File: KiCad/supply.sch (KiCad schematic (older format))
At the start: 75 parts, among them IC10 AP62301Z6-7, IC12 74HC00PW, IC13 SN74LVC1G126DCKR, IC3 TPS54561, IC4 TPS7A0518PDBVT, IC8 LM3671MF-3.3, IC9 LM3671MF-3.3, T3 BSS138APW

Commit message: Replace 5V0 and 3V3 DCDC
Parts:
- removed C16, C17, C18: C_47u_0805, jetson-nano-baseboard-footprints:0805-cap, symbol jetson-nano-baseboard:C_47u_0805
- removed C19: C_100n_0402, jetson-nano-baseboard-footprints:0402-cap, symbol jetson-nano-baseboard:C_100n_0402
- removed C20, C59, C61: C_22u_0603, antmicro-footprints:0603-cap, symbol antmicroCapacitors0603:C_22u_0603
- removed C21, C22, C23: C_2u2_1206, jetson-nano-baseboard-footprints:1206-cap, symbol jetson-nano-baseboard:C_2u2_1206
- removed C24: C_10n_0402, jetson-nano-baseboard-footprints:0402-cap, symbol jetson-nano-baseboard:C_10n_0402
- removed C25: C_4n7_0402, jetson-nano-baseboard-footprints:0402-cap, symbol jetson-nano-baseboard:C_4n7_0402
- removed C28: C_100n_0402, antmicro-footprints:0402-cap, symbol antmicroCapacitors0402:C_100n_0402
- removed C55, C57: C_2u2_0402, jetson-nano-baseboard-footprints:0402-cap, symbol jetson-nano-baseboard:C_2u2_0402
- removed C56, C58: C_10u_0603, jetson-nano-baseboard-footprints:0603-cap, symbol jetson-nano-baseboard:C_10u_0603
- removed C64: C_47p_0402, jetson-nano-baseboard-footprints:0402-cap, symbol jetson-nano-baseboard:C_47p_0402
- removed D1: PDS760-13, jetson-nano-baseboard-footprints:PowerDI, symbol jetson-nano-baseboard:Diode_Schottky
- removed FB1: 742792022, antmicro-footprints:0805-cap, symbol Device:Ferrite_Bead_Small
- removed IC10: AP62301Z6-7, antmicro-footprints:SOT-563, symbol antmicroDCDCConverters:AP62301Z6-7
- removed IC3: TPS54561, jetson-nano-baseboard-footprints:WSON-10_4x4, symbol jetson-nano-baseboard:TPS54561
- removed IC8, IC9: LM3671MF-3.3, jetson-nano-baseboard-footprints:SOT23-5N, symbol jetson-nano-baseboard:LM3671
- removed L1: WE_7447798720, jetson-nano-baseboard-footprints:WE_7447798720, symbol jetson-nano-baseboard:WE_7447798720
- removed L4, L6: LQH32PN2R2NN0L, jetson-nano-baseboard-footprints:LQH32PN2R2NN0L, symbol jetson-nano-baseboard:LQH32PN2R2NN0L
- removed L5: XEL4030-332MEC, antmicro-footprints:Coilcraft-XEL4030, symbol antmicroFixedInductors:XEL4030-332MEC
- removed R134: R_33k2_0402, antmicro-footprints:0402-res, symbol antmicroResistors0402:R_33k2_0402
- removed R44: R_243k_0402, jetson-nano-baseboard-footprints:0402-res, symbol jetson-nano-baseboard:R_243k_0402
- removed R45: R_49R9_0402, jetson-nano-baseboard-footprints:0402-res, symbol jetson-nano-baseboard:R_49R9_0402
- removed R46: R_53k6_0402, jetson-nano-baseboard-footprints:0402-res, symbol jetson-nano-baseboard:R_53k6_0402
- removed R48: R_16k9_0402, jetson-nano-baseboard-footprints:0402-res, symbol jetson-nano-baseboard:R_16k9_0402
- removed R52: R_10k2_0402, jetson-nano-baseboard-footprints:0402-res, symbol jetson-nano-baseboard:R_10k2_0402
- removed R74: R_0R_0402, antmicro-footprints:0402-res, symbol antmicroResistors0402:R_0R_0402
- removed R75, R76: R_10k_0402, antmicro-footprints:0402-res, symbol antmicroResistors0402:R_10k_0402
- removed R77: R_100k_0402, jetson-nano-baseboard-footprints:0402-res, symbol jetson-nano-baseboard:R_100k_0402
- removed R89, R91: R_0R_0402, jetson-nano-baseboard-footprints:0402-res, symbol jetson-nano-baseboard:R_0R_0402
- removed R90, R93: R_10k_0402, jetson-nano-baseboard-footprints:0402-res, symbol jetson-nano-baseboard:R_10k_0402
- removed TP41, TP43, TP45, TP5: ~, jetson-nano-baseboard-footprints:TP-R-1.5, symbol jetson-nano-baseboard:Testpad
- added C81, C82: C_4u7_0603, antmicro-footprints:0603-cap, symbol antmicroCapacitors0603:C_4u7_0603
- added C83, C84, C85, C86: C_220n_0603_25V, antmicro-footprints:0603-cap, symbol antmicroCapacitors0603:C_220n_0603_25V
- added C87, C88: C_1u_0402, antmicro-footprints:0402-cap, symbol antmicroCapacitors0402:C_1u_0402
- added C89, C90: C_100n_0402, antmicro-footprints:0402-cap, symbol antmicroCapacitors0402:C_100n_0402
- added C91, C94, C95, C96, C97, C98: C_47u_0603, antmicro-footprints:0603-cap, symbol antmicroCapacitors0603:C_47u_0603
- added C92, C93: C_15p_0402, antmicro-footprints:0402-cap, symbol antmicroCapacitors0402:C_15p_0402
- added FB3, FB4: 742792022, antmicro-footprints:0805-cap, symbol Device:Ferrite_Bead_Small
- added L11: 7447709150, antmicro-footprints:WE_7447709150, symbol antmicroFixedInductors:7447709150
- added L12: 7443251000, antmicro-footprints:WE_7443251000, symbol antmicroFixedInductors:7443251000
- added R117, R94: R_100k_0402, antmicro-footprints:0402-res, symbol antmicroResistors0402:R_100k_0402
- added R118, R120: R_100k_1%_0402, antmicro-footprints:0402, symbol antmicroResistors0402:R_100k_1%_0402
- added R119: R_44k2_0402, antmicro-footprints:0402-res, symbol antmicroResistors0402:R_44k2_0402
- added R121: R_24k9_0.1%_0402, antmicro-footprints:0402-res, symbol antmicroResistors0402:R_24k9_0.1%_0402
- added R?: R_10k_0402, jetson-nano-baseboard-footprints:0402-res, symbol jetson-nano-baseboard:R_10k_0402
- added R?: R_0R_0402, jetson-nano-baseboard-footprints:0402-res, symbol jetson-nano-baseboard:R_0R_0402
- added U1, U2: LM60440AQRPKRQ1, LM60440AQRPKRQ1, symbol antmicroDCDCConverters:LM60440AQRPKRQ1
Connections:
- wire segments 229 -> 192
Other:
- note added: "3V3 DC/DC"
- note added: "3V3/4A"
- note added: "5V DC/DC"
- note added: "5V/4A"
- note removed: "5V/5A"
- note removed: "Bulk load"
- note removed: "Camera #1 3V3"
- note removed: "Camera #2 3V3"
- note removed: "Main DC/DC"
- note removed: "System 3V3"
- moved on the sheet: C60, C65, IC4, R92, TP40, TP47

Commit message: Fix symbols, change DCDCC output capacitors to 0805
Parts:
- removed C91, C94, C95, C96, C97, C98: C_47u_0603, antmicro-footprints:0603-cap, symbol antmicroCapacitors0603:C_47u_0603
- added C? (x6): C_47u_0805, antmicro-footprints:0805-cap, symbol antmicroCapacitorsmisc:C_47u_0805
- gave numbers to parts that had none: 2
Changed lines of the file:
@@
 Wire Wire Line
 	4050 3150 5025 3150
-$Comp
-L antmicroCapacitors0603:C_47u_0603 C94
-U 1 1 619E2469
-P 5150 2025
-F 0 "C94" H 5265 2070 60  0000 L CNN
-F 1 "C_47u_0603" H 5150 1875 60  0001 C CNN
-F 2 "antmicro-footprints:0603-cap" H 5350 2225 60  0001 L CNN
-F 3 "" H 5150 2025 50  0001 C CNN
-F 4 "MURATA" H 5350 2425 60  0001 L CNN "Manufacturer"
-F 5 "GRM188R60J476ME15D" H 5350 2325 60  0001 L CNN "MPN"
-F 6 "47u" H 5265 1972 50  0000 L CNN "Val"
-	1    5150 2025
-	1    0    0    -1
-$EndComp
 Text GLabel 5575 2500 2    50   Input ~ 0
 5V0_SYS
@@
 Text GLabel 5125 1875 0    50   Input ~ 0
 5V0_SYS
-Wire Wire Line
-	5125 1875 5150 1875
-Connection ~ 5150 1875
 $Comp
 L Device:Ferrite_Bead_Small FB4
@@
 	4000 5800 4975 5800
 $Comp
-L antmicroCapacitors0603:C_47u_0603 C91
-U 1 1 61E2F969
-P 4900 4650
-F 0 "C91" H 5015 4695 60  0000 L CNN
-F 1 "C_47u_0603" H 4900 4500 60  0001 C CNN
-F 2 "antmicro-footprints:0603-cap" H 5100 4850 60  0001 L CNN
-F 3 "" H 4900 4650 50  0001 C CNN
-F 4 "MURATA" H 5100 5050 60  0001 L CNN "Manufacturer"
-F 5 "GRM188R60J476ME15D" H 5100 4950 60  0001 L CNN "MPN"
-F 6 "47u" H 5015 4597 50  0000 L CNN "Val"
-	1    4900 4650
-	1    0    0    -1
-$EndComp
-$Comp
 L jetson-nano-baseboard:GND #GND_0163
 U 1 1 61E2F985
@@
 	1975 4850 1550 4850
 Connection ~ 5325 5150
-Wire Wire Line
-	4875 4500 4900 4500
-Connection ~ 4900 4500
 $Comp
 L Device:Ferrite_Bead_Small FB3
@@
 #RESET
 $Comp
-L jetson-nano-baseboard:R_10k_0402 R?
+L jetson-nano-baseboard:R_10k_0402 R44
 U 1 1 620FA0ED
 P 2200 5550
-F 0 "R?" H 2200 5450 60  0000 C CNN
+F 0 "R44" H 2200 5450 60  0000 C CNN
 F 1 "R_10k_0402" H 2200 5400 60  0001 C CNN
 F 2 "jetson-nano-baseboard-footprints:0402-res" H 2400 5750 60  0001 L CNN
@@
 	2350 5550 2675 5550
 $Comp
-L jetson-nano-baseboard:R_0R_0402 R?
+L jetson-nano-baseboard:R_0R_0402 R45
 U 1 1 6216200E
 P 2675 5250
-F 0 "R?" V 2766 5320 60  0000 L CNN
+F 0 "R45" V 2766 5320 60  0000 L CNN
 F 1 "R_0R_0402" H 2675 5100 60  0001 C CNN
 F 2 "jetson-nano-baseboard-footprints:0402-res" H 2875 5450 60  0001 L CNN
@@
 $EndComp
 $Comp
-L antmicroCapacitors0603:C_47u_0603 C96
-U 1 1 61A02D24
-P 5600 2025
-F 0 "C96" H 5715 2070 60  0000 L CNN
-F 1 "C_47u_0603" H 5600 1875 60  0001 C CNN
-F 2 "antmicro-footprints:0603-cap" H 5800 2225 60  0001 L CNN
-F 3 "" H 5600 2025 50  0001 C CNN
-F 4 "MURATA" H 5800 2425 60  0001 L CNN "Manufacturer"
-F 5 "GRM188R60J476ME15D" H 5800 2325 60  0001 L CNN "MPN"
-F 6 "47u" H 5715 1972 50  0000 L CNN "Val"
-	1    5600 2025
-	1    0    0    -1
-$EndComp
-$Comp
-L antmicroCapacitors0603:C_47u_0603 C98
-U 1 1 61A14F82
-P 6025 2025
-F 0 "C98" H 6140 2070 60  0000 L CNN
-F 1 "C_47u_0603" H 6025 1875 60  0001 C CNN
-F 2 "antmicro-footprints:0603-cap" H 6225 2225 60  0001 L CNN
-F 3 "" H 6025 2025 50  0001 C CNN
-F 4 "MURATA" H 6225 2425 60  0001 L CNN "Manufacturer"
-F 5 "GRM188R60J476ME15D" H 6225 2325 60  0001 L CNN "MPN"
-F 6 "47u" H 6140 1972 50  0000 L CNN "Val"
-	1    6025 2025
-	1    0    0    -1
-$EndComp
-$Comp
 L jetson-nano-baseboard:GND #GND_0156
 U 1 1 61AC273D
@@
 	1    0    0    -1
 $EndComp
-Connection ~ 5600 1875
-Wire Wire Line
-	5150 1875 5600 1875
-Wire Wire Line
-	5600 1875 6025 1875
-$Comp
-L antmicroCapacitors0603:C_47u_0603 C95
-U 1 1 61E2F972
-P 5350 4650
-F 0 "C95" H 5465 4695 60  0000 L CNN
-F 1 "C_47u_0603" H 5350 4500 60  0001 C CNN
-F 2 "antmicro-footprints:0603-cap" H 5550 4850 60  0001 L CNN
-F 3 "" H 5350 4650 50  0001 C CNN
-F 4 "MURATA" H 5550 5050 60  0001 L CNN "Manufacturer"
-F 5 "GRM188R60J476ME15D" H 5550 4950 60  0001 L CNN "MPN"
-F 6 "47u" H 5465 4597 50  0000 L CNN "Val"
-	1    5350 4650
-	1    0    0    -1
-$EndComp
-$Comp
-L antmicroCapacitors0603:C_47u_0603 C97
-U 1 1 61E2F97B
-P 5775 4650
-F 0 "C97" H 5890 4695 60  0000 L CNN
-F 1 "C_47u_0603" H 5775 4500 60  0001 C CNN
-F 2 "antmicro-footprints:0603-cap" H 5975 4850 60  0001 L CNN
-F 3 "" H 5775 4650 50  0001 C CNN
-F 4 "MURATA" H 5975 5050 60  0001 L CNN "Manufacturer"
-F 5 "GRM188R60J476ME15D" H 5975 4950 60  0001 L CNN "MPN"
-F 6 "47u" H 5890 4597 50  0000 L CNN "Val"
-	1    5775 4650
-	1    0    0    -1
-$EndComp
 $Comp
 L jetson-nano-baseboard:GND #GND_0165
@@
 $EndComp
 Wire Wire Line
-	5350 4500 5775 4500
-Wire Wire Line
-	4900 4500 5350 4500
-Connection ~ 5350 4500
-Wire Wire Line
 	4000 5550 4400 5550
 Text Notes 1250 4175 0    59   ~ 12
@@
 Text Notes 1250 4300 0    59   ~ 12
 3V3/4A
+$Comp
+L antmicroCapacitorsmisc:C_47u_0805 C?
+U 1 1 624E69E4
+P 4900 4650
+F 0 "C?" H 5015 4695 60  0000 L CNN
+F 1 "C_47u_0805" H 4900 4500 60  0001 C CNN
+F 2 "antmicro-footprints:0805-cap" H 5100 4850 60  0001 L CNN
+F 3 "" H 4900 4650 50  0001 C CNN
+F 4 "KEMET" H 5100 5050 60  0001 L CNN "Manufacturer"
+F 5 "C0805C476M9PACTU" H 5100 4950 60  0001 L CNN "MPN"
+F 6 "47u" H 5015 4597 50  0000 L CNN "Val"
+	1    4900 4650
+	1    0    0    -1
+$EndComp
+Wire Wire Line
+	4875 4500 4900 4500
+Connection ~ 4900 4500
+$Comp
+L antmicroCapacitorsmisc:C_47u_0805 C?
+U 1 1 624FD21A
+P 5350 4650
+F 0 "C?" H 5465 4695 60  0000 L CNN
+F 1 "C_47u_0805" H 5350 4500 60  0001 C CNN
+F 2 "antmicro-footprints:0805-cap" H 5550 4850 60  0001 L CNN
+F 3 "" H 5350 4650 50  0001 C CNN
+F 4 "KEMET" H 5550 5050 60  0001 L CNN "Manufacturer"
+F 5 "C0805C476M9PACTU" H 5550 4950 60  0001 L CNN "MPN"
+F 6 "47u" H 5465 4597 50  0000 L CNN "Val"
+	1    5350 4650
+	1    0    0    -1
+$EndComp
+$Comp
+L antmicroCapacitorsmisc:C_47u_0805 C?
+U 1 1 62508FB8
+P 5775 4650
+F 0 "C?" H 5890 4695 60  0000 L CNN
+F 1 "C_47u_0805" H 5775 4500 60  0001 C CNN
+F 2 "antmicro-footprints:0805-cap" H 5975 4850 60  0001 L CNN
+F 3 "" H 5775 4650 50  0001 C CNN
+F 4 "KEMET" H 5975 5050 60  0001 L CNN "Manufacturer"
+F 5 "C0805C476M9PACTU" H 5975 4950 60  0001 L CNN "MPN"
+F 6 "47u" H 5890 4597 50  0000 L CNN "Val"
+	1    5775 4650
+	1    0    0    -1
+$EndComp
+$Comp
+L antmicroCapacitorsmisc:C_47u_0805 C?
+U 1 1 62515712
+P 5150 2025
+F 0 "C?" H 5265 2070 60  0000 L CNN
+F 1 "C_47u_0805" H 5150 1875 60  0001 C CNN
+F 2 "antmicro-footprints:0805-cap" H 5350 2225 60  0001 L CNN
+F 3 "" H 5150 2025 50  0001 C CNN
+F 4 "KEMET" H 5350 2425 60  0001 L CNN "Manufacturer"
+F 5 "C0805C476M9PACTU" H 5350 2325 60  0001 L CNN "MPN"
+F 6 "47u" H 5265 1972 50  0000 L CNN "Val"
+	1    5150 2025
+	1    0    0    -1
+$EndComp
+$Comp
+L antmicroCapacitorsmisc:C_47u_0805 C?
+U 1 1 62521314
+P 5600 2025
+F 0 "C?" H 5715 2070 60  0000 L CNN
+F 1 "C_47u_0805" H 5600 1875 60  0001 C CNN
+F 2 "antmicro-footprints:0805-cap" H 5800 2225 60  0001 L CNN
+F 3 "" H 5600 2025 50  0001 C CNN
+F 4 "KEMET" H 5800 2425 60  0001 L CNN "Manufacturer"
+F 5 "C0805C476M9PACTU" H 5800 2325 60  0001 L CNN "MPN"
+F 6 "47u" H 5715 1972 50  0000 L CNN "Val"
+	1    5600 2025
+	1    0    0    -1
+$EndComp
+$Comp
+L antmicroCapacitorsmisc:C_47u_0805 C?
+U 1 1 6252D09E
+P 6025 2025
+F 0 "C?" H 6140 2070 60  0000 L CNN
+F 1 "C_47u_0805" H 6025 1875 60  0001 C CNN
+F 2 "antmicro-footprints:0805-cap" H 6225 2225 60  0001 L CNN
+F 3 "" H 6025 2025 50  0001 C CNN
+F 4 "KEMET" H 6225 2425 60  0001 L CNN "Manufacturer"
+F 5 "C0805C476M9PACTU" H 6225 2325 60  0001 L CNN "MPN"
+F 6 "47u" H 6140 1972 50  0000 L CNN "Val"
+	1    6025 2025
+	1    0    0    -1
+$EndComp
+Wire Wire Line
+	5125 1875 5150 1875
+Connection ~ 5150 1875
+Wire Wire Line
+	5150 1875 5600 1875
+Connection ~ 5600 1875
+Wire Wire Line
+	5600 1875 6025 1875
+Wire Wire Line
+	4900 4500 5350 4500
+Connection ~ 5350 4500
+Wire Wire Line
+	5350 4500 5775 4500
 $EndSCHEMATC

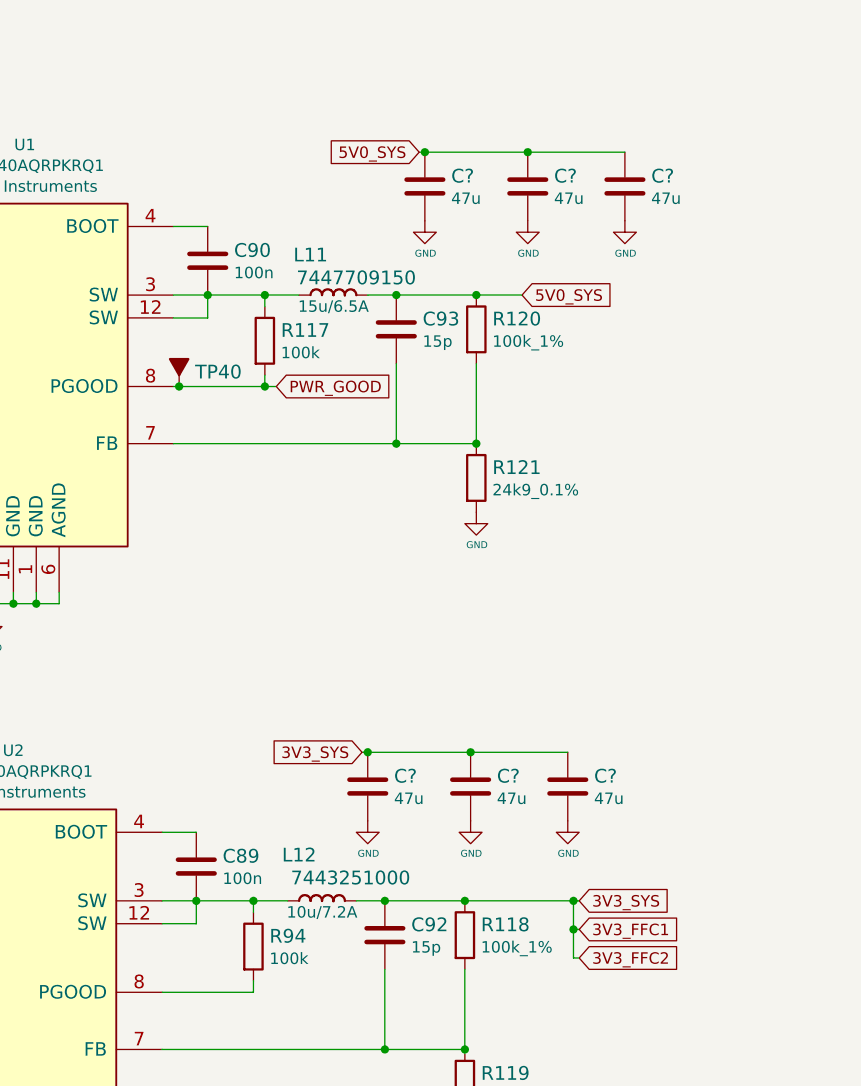
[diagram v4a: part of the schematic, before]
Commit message: Disconnect pin 3 and 12 of LM604x0. Based on layout from datasheet
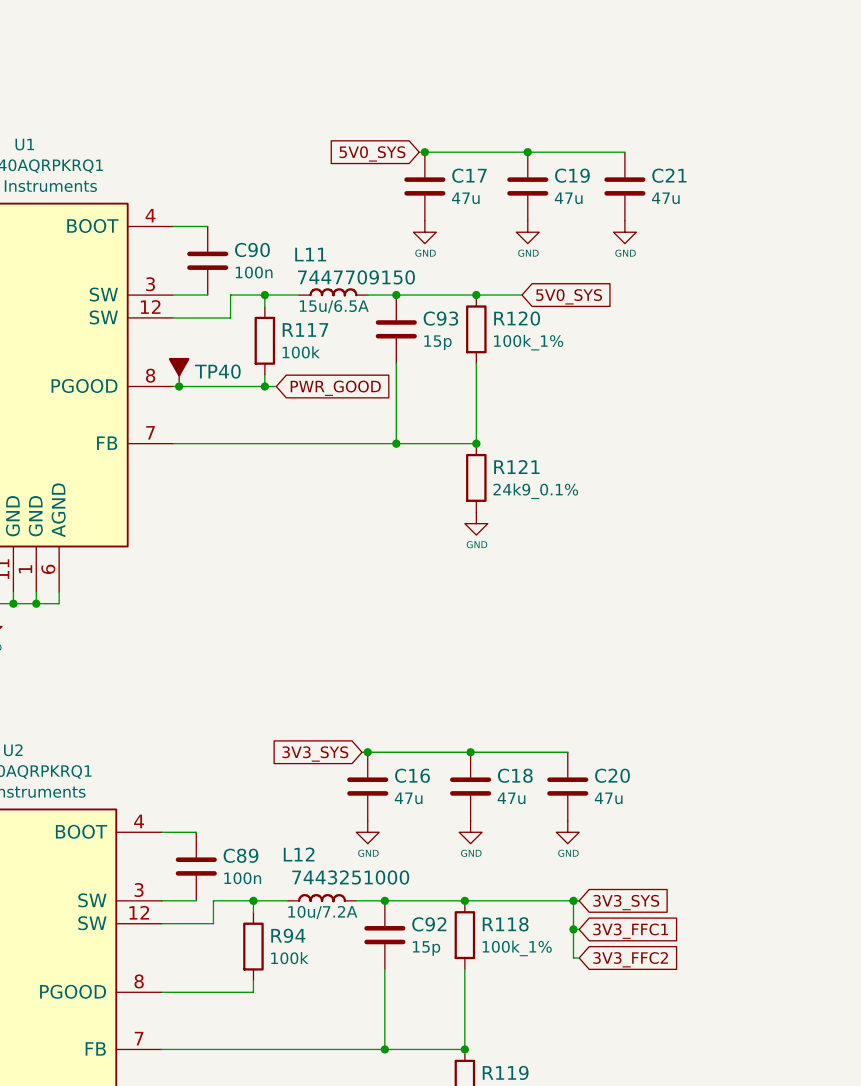
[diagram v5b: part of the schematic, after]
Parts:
- gave numbers to parts that had none: 6
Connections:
- net at L11.1 (P), R117.1, U1.12 (SW): no longer C90.1, U1.3 (SW)
- net at L12.1 (P), R94.1, U2.12 (SW): no longer C89.1, U2.3 (SW)
- new net: C90.1, U1.3 (SW)
- new net: C89.1, U2.3 (SW)
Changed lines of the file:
@@
 Wire Wire Line
 	4050 2500 4200 2500
-Wire Wire Line
-	4200 2500 4450 2500
-Connection ~ 4200 2500
-Wire Wire Line
-	4200 2600 4200 2500
-Wire Wire Line
-	4050 2600 4200 2600
 Text GLabel 4500 2900 2    50   Input ~ 0
 PWR_GOOD
@@
 Wire Wire Line
 	4075 2900 4450 2900
-Connection ~ 4450 2500
 Connection ~ 4450 2900
 Wire Wire Line
@@
 Wire Wire Line
 	4000 5150 4150 5150
-Wire Wire Line
-	4150 5150 4400 5150
-Connection ~ 4150 5150
-Wire Wire Line
-	4150 5250 4150 5150
-Wire Wire Line
-	4000 5250 4150 5250
 $Comp
 L antmicroResistors0402:R_100k_0402 R94
@@
 Wire Wire Line
 	5325 5450 5325 5800
-Connection ~ 4400 5150
 Wire Wire Line
 	4400 5150 4550 5150
@@
 3V3/4A
 $Comp
-L antmicroCapacitorsmisc:C_47u_0805 C?
+L antmicroCapacitorsmisc:C_47u_0805 C16
 U 1 1 624E69E4
 P 4900 4650
-F 0 "C?" H 5015 4695 60  0000 L CNN
+F 0 "C16" H 5015 4695 60  0000 L CNN
 F 1 "C_47u_0805" H 4900 4500 60  0001 C CNN
 F 2 "antmicro-footprints:0805-cap" H 5100 4850 60  0001 L CNN
@@
 Connection ~ 4900 4500
 $Comp
-L antmicroCapacitorsmisc:C_47u_0805 C?
+L antmicroCapacitorsmisc:C_47u_0805 C18
 U 1 1 624FD21A
 P 5350 4650
-F 0 "C?" H 5465 4695 60  0000 L CNN
+F 0 "C18" H 5465 4695 60  0000 L CNN
 F 1 "C_47u_0805" H 5350 4500 60  0001 C CNN
 F 2 "antmicro-footprints:0805-cap" H 5550 4850 60  0001 L CNN
@@
 $EndComp
 $Comp
-L antmicroCapacitorsmisc:C_47u_0805 C?
+L antmicroCapacitorsmisc:C_47u_0805 C20
 U 1 1 62508FB8
 P 5775 4650
-F 0 "C?" H 5890 4695 60  0000 L CNN
+F 0 "C20" H 5890 4695 60  0000 L CNN
 F 1 "C_47u_0805" H 5775 4500 60  0001 C CNN
 F 2 "antmicro-footprints:0805-cap" H 5975 4850 60  0001 L CNN
@@
 $EndComp
 $Comp
-L antmicroCapacitorsmisc:C_47u_0805 C?
+L antmicroCapacitorsmisc:C_47u_0805 C17
 U 1 1 62515712
 P 5150 2025
-F 0 "C?" H 5265 2070 60  0000 L CNN
+F 0 "C17" H 5265 2070 60  0000 L CNN
 F 1 "C_47u_0805" H 5150 1875 60  0001 C CNN
 F 2 "antmicro-footprints:0805-cap" H 5350 2225 60  0001 L CNN
@@
 $EndComp
 $Comp
-L antmicroCapacitorsmisc:C_47u_0805 C?
+L antmicroCapacitorsmisc:C_47u_0805 C19
 U 1 1 62521314
 P 5600 2025
-F 0 "C?" H 5715 2070 60  0000 L CNN
+F 0 "C19" H 5715 2070 60  0000 L CNN
 F 1 "C_47u_0805" H 5600 1875 60  0001 C CNN
 F 2 "antmicro-footprints:0805-cap" H 5800 2225 60  0001 L CNN
@@
 $EndComp
 $Comp
-L antmicroCapacitorsmisc:C_47u_0805 C?
+L antmicroCapacitorsmisc:C_47u_0805 C21
 U 1 1 6252D09E
 P 6025 2025
-F 0 "C?" H 6140 2070 60  0000 L CNN
+F 0 "C21" H 6140 2070 60  0000 L CNN
 F 1 "C_47u_0805" H 6025 1875 60  0001 C CNN
 F 2 "antmicro-footprints:0805-cap" H 6225 2225 60  0001 L CNN
@@
 Wire Wire Line
 	5350 4500 5775 4500
+Wire Wire Line
+	4225 5250 4225 5150
+Wire Wire Line
+	4225 5150 4400 5150
+Wire Wire Line
+	4000 5250 4225 5250
+Connection ~ 4400 5150
+Wire Wire Line
+	4300 2600 4300 2500
+Wire Wire Line
+	4300 2500 4450 2500
+Wire Wire Line
+	4050 2600 4300 2600
+Connection ~ 4450 2500
 $EndSCHEMATC
